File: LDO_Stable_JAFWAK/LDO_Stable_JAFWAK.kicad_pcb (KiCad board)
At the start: 4 copper layers, 1 part, among them U1 SU272AFJK_LDO

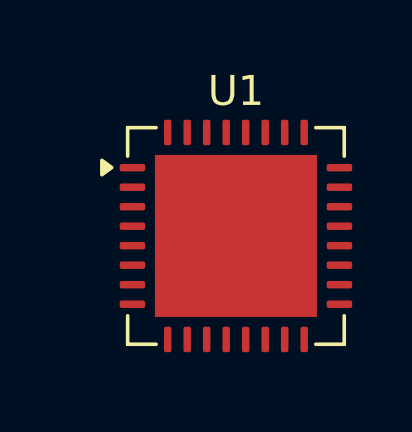
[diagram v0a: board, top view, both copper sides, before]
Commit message: Updated pin assignments on footprint
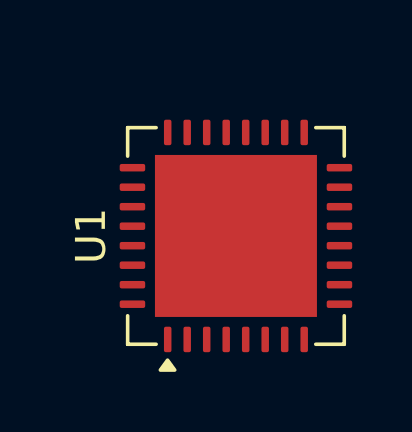
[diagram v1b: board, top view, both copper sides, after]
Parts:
- turned U1 to 90 degrees
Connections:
- U1 pad 1: BGR_VDD -> EN_VDD
- U1 pad 10: BGR_VDD -> VSS
- U1 pad 11: Net-(U1-EN_AIN) -> OTA_VDD
- U1 pad 12: Net-(U1-EN_AIN) -> OTA_VDD
- U1 pad 13: Net-(U1-EN_AIN) -> Net-(U1-VOUT-Pad13)
- U1 pad 14: Net-(U1-EN_AIN) -> Net-(U1-VOUT-Pad13)
- U1 pad 15: Net-(U1-EN_AIN) -> VSS
- U1 pad 16: BGR_VDD -> VDD
- U1 pad 17: BGR_VDD -> VDD
- U1 pad 18: BGR_VDD -> VDD
- U1 pad 19: BGR_VDD -> VDD
- U1 pad 2: BGR_VDD -> EN_VDD
- U1 pad 20: BGR_VDD -> VSS
- U1 pad 21: Net-(U1-EN_AIN) -> unconnected-(U1-VREF_IN-Pad21)
- U1 pad 22: Net-(U1-EN_AIN) -> VSS
- U1 pad 23: BGR_VDD -> unconnected-(U1-VREF_OUT-Pad23)
- U1 pad 24: BGR_VDD -> VDD
- U1 pad 27: BGR_VDD -> unconnected-(U1-VMIRROR-Pad27)
- U1 pad 28: BGR_VDD -> VSS
- U1 pad 29: Net-(U1-EN_AIN) -> VSS
- U1 pad 3: Net-(U1-EN_AIN) -> unconnected-(U1-EN_AIN-Pad3)
- U1 pad 30: BGR_VDD -> VSS
- U1 pad 31: Net-(U1-EN_AIN) -> VSS
- U1 pad 32: BGR_VDD -> VDD
- U1 pad 4: BGR_VDD -> unconnected-(U1-EN_OUT-Pad4)
- U1 pad 5: BGR_VDD -> unconnected-(U1-~{EN_OUT}-Pad5)
- U1 pad 6: BGR_VDD -> unconnected-(U1-~{EN_IN}-Pad6)
- U1 pad 7: BGR_VDD -> unconnected-(U1-EN_IN-Pad7)
- U1 pad 8: BGR_VDD -> VDD
- U1 pad 9: BGR_VDD -> VSS

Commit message: Built out primary systems
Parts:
- added C1: 0.1nF, Capacitor_SMD:C_0805_2012Metric_Pad1.18x1.45mm_HandSolder, F.Cu at (31.2, 12.7)
- added C10: 1nF, Capacitor_SMD:C_0805_2012Metric_Pad1.18x1.45mm_HandSolder, F.Cu at (40.8, 15.7)
- added C11: 100uF, TPS7A7001_Evaluation_Board_footprint_lib:CAPPRD350W60D800H1150, F.Cu at (34.2, 28.0)
- added C12: 1nF, Capacitor_SMD:C_0805_2012Metric_Pad1.18x1.45mm_HandSolder, F.Cu at (40.8, 18.7)
- added C13: 10uF, Capacitor_SMD:C_0805_2012Metric_Pad1.18x1.45mm_HandSolder, F.Cu at (40.8, 21.7)
- added C2: 100nF, Capacitor_SMD:C_0805_2012Metric_Pad1.18x1.45mm_HandSolder, F.Cu at (31.2, 15.7)
- added C3: 10uF, Capacitor_SMD:C_0805_2012Metric_Pad1.18x1.45mm_HandSolder, F.Cu at (31.2, 18.7)
- added C4: 10uF, Capacitor_SMD:C_0805_2012Metric_Pad1.18x1.45mm_HandSolder, F.Cu at (31.2, 21.7)
- added C5: 100nF, Capacitor_SMD:C_0805_2012Metric_Pad1.18x1.45mm_HandSolder, F.Cu at (36.0, 12.7)
- added C6: 0.1nF, Capacitor_SMD:C_0805_2012Metric_Pad1.18x1.45mm_HandSolder, F.Cu at (36.0, 15.7)
- added C7: OPEN, Capacitor_SMD:C_0805_2012Metric_Pad1.18x1.45mm_HandSolder, F.Cu at (36.0, 18.7)
- added C8: 1nF, Capacitor_SMD:C_0805_2012Metric_Pad1.18x1.45mm_HandSolder, F.Cu at (36.0, 21.7)
- added C9: 1nF, Capacitor_SMD:C_0805_2012Metric_Pad1.18x1.45mm_HandSolder, F.Cu at (40.8, 12.7)
- added H1: MountingHole, MountingHole:MountingHole_2.5mm, F.Cu at (11.8, 14.5)
- added H2: MountingHole, MountingHole:MountingHole_2.5mm, F.Cu at (11.8, 21.0)
- added H3: MountingHole, MountingHole:MountingHole_2.5mm, F.Cu at (11.8, 27.6)
- added H4: MountingHole, MountingHole:MountingHole_2.5mm, F.Cu at (11.8, 34.1)
- added J11: TMP_OUT, TPS7A7001_Evaluation_Board_footprint_lib:CONN_PxC02S_SUL, F.Cu at (19.4, 24.5)
- added J13: V_SIG, TPS7A7001_Evaluation_Board_footprint_lib:SAMTEC_SMA-J-P-H-ST-TH1, F.Cu at (4.01, 42.8)
- added J5: FILT_IN, TPS7A7001_Evaluation_Board_footprint_lib:CONN_PxC02S_SUL, F.Cu at (19.4, 14.2)
- added J6: FILT_OUT, TPS7A7001_Evaluation_Board_footprint_lib:CONN_PxC02S_SUL, F.Cu at (19.4, 19.4)
- added J7: IN_S, TPS7A7001_Evaluation_Board_footprint_lib:SAMTEC_SMA-J-P-H-ST-TH1, F.Cu at (4.01, 15.7)
- added J8: OUT_S, TPS7A7001_Evaluation_Board_footprint_lib:SAMTEC_SMA-J-P-H-ST-TH1, F.Cu at (4.01, 24.8)
- added J9: FILT_IN_S, TPS7A7001_Evaluation_Board_footprint_lib:SAMTEC_SMA-J-P-H-ST-TH1, F.Cu at (4.01, 33.8)
- added JP1: PEC03SAAN, TPS7A7001_Evaluation_Board_footprint_lib:CONN_PEC03SAAN_SUL, F.Cu at (39.9, 34.9)
- added JP2: TMP, TPS7A7001_Evaluation_Board_footprint_lib:CONN_PxC02S_SUL, F.Cu at (19.4, 29.7)
- added JP3: BW_ADJ, TPS7A7001_Evaluation_Board_footprint_lib:CONN_PxC02S_SUL, F.Cu at (19.4, 34.8)
- added R1: R, Package_DIP:DIP-8_W7.62mm, F.Cu at (1.08, 1.54)
- added R10: 10k, Resistor_SMD:R_0805_2012Metric_Pad1.20x1.40mm_HandSolder, F.Cu at (26.4, 21.5)
- added R11: 10k, Resistor_SMD:R_0805_2012Metric_Pad1.20x1.40mm_HandSolder, F.Cu at (26.4, 24.5)
- added R12: 30k, Resistor_SMD:R_0805_2012Metric_Pad1.20x1.40mm_HandSolder, F.Cu at (26.4, 27.4)
- added R13: 30k, Resistor_SMD:R_0805_2012Metric_Pad1.20x1.40mm_HandSolder, F.Cu at (26.4, 30.4)
- added R14: 100m, Resistor_SMD:R_2512_6332Metric_Pad1.40x3.35mm_HandSolder, F.Cu at (33.3, 40.2)
- added R15: 0, Resistor_SMD:R_0805_2012Metric_Pad1.20x1.40mm_HandSolder, F.Cu at (26.4, 33.3)
- added R2: R, Package_DIP:DIP-8_W7.62mm, F.Cu at (11.9, 1.54)
- added R3: R, Package_DIP:DIP-8_W7.62mm, F.Cu at (22.6, 1.54)
- added R4: R, Package_DIP:DIP-8_W7.62mm, F.Cu at (33.4, 1.54)
- added R5: R, Package_DIP:DIP-8_W7.62mm, F.Cu at (44.2, 1.54)
- added R6: 10k, Resistor_SMD:R_0805_2012Metric_Pad1.20x1.40mm_HandSolder, F.Cu at (26.4, 12.7)
- added R7: 10k, Resistor_SMD:R_0805_2012Metric_Pad1.20x1.40mm_HandSolder, F.Cu at (26.4, 15.6)
- added R8: 10k, Resistor_SMD:R_0805_2012Metric_Pad1.20x1.40mm_HandSolder, F.Cu at (26.4, 18.6)
- added R9: 100m, Resistor_SMD:R_2512_6332Metric_Pad1.40x3.35mm_HandSolder, F.Cu at (33.3, 35.3)
- added U2: TMP235A2DBZR, TPS7A7001_Evaluation_Board_footprint_lib:DBZ0003A-IPC_A, F.Cu at (50.3, 25.3)
- added U3: TPS7A7001DDAR, TPS7A7001_Evaluation_Board_footprint_lib:DDA0008E-IPC_A, F.Cu at (42.8, 41.0)
- added U4: BUF634AIDR, TPS7A7001_Evaluation_Board_footprint_lib:SOIC127P599X175-8N, F.Cu at (43.7, 26.5)
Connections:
- U1 pad 27: unconnected-(U1-VMIRROR-Pad27) -> VDD

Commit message: Roughed In schematic
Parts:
- removed C10, C8, C9: 1nF, Capacitor_SMD:C_0805_2012Metric_Pad1.18x1.45mm_HandSolder
- removed C4: 10uF, Capacitor_SMD:C_0805_2012Metric_Pad1.18x1.45mm_HandSolder
- removed C5: 100nF, Capacitor_SMD:C_0805_2012Metric_Pad1.18x1.45mm_HandSolder
- removed J11: TMP_OUT, TPS7A7001_Evaluation_Board_footprint_lib:CONN_PxC02S_SUL
- removed J13: V_SIG, TPS7A7001_Evaluation_Board_footprint_lib:SAMTEC_SMA-J-P-H-ST-TH1
- removed J7: IN_S, TPS7A7001_Evaluation_Board_footprint_lib:SAMTEC_SMA-J-P-H-ST-TH1
- removed J9: FILT_IN_S, TPS7A7001_Evaluation_Board_footprint_lib:SAMTEC_SMA-J-P-H-ST-TH1
- removed JP1: PEC03SAAN, TPS7A7001_Evaluation_Board_footprint_lib:CONN_PEC03SAAN_SUL
- removed R1, R2, R3, R4, R5: R, Package_DIP:DIP-8_W7.62mm
- removed R11, R6, R7, R8: 10k, Resistor_SMD:R_0805_2012Metric_Pad1.20x1.40mm_HandSolder
- removed R15: 0, Resistor_SMD:R_0805_2012Metric_Pad1.20x1.40mm_HandSolder
- removed U3: TPS7A7001DDAR, TPS7A7001_Evaluation_Board_footprint_lib:DDA0008E-IPC_A
- removed U4: BUF634AIDR, TPS7A7001_Evaluation_Board_footprint_lib:SOIC127P599X175-8N
- added C14: 100n, Capacitor_SMD:C_0805_2012Metric_Pad1.18x1.45mm_HandSolder, F.Cu at (159.3, 161.5)
- added C15: 100n, Capacitor_SMD:C_0805_2012Metric_Pad1.18x1.45mm_HandSolder, F.Cu at (143.1, 177.4)
- added C16: 100uF, TPS7A7001_Evaluation_Board_footprint_lib:CAPPRD350W60D800H1150, F.Cu at (91.3, 83.6)
- added J1: VIN_DC, TPS7A7001_Evaluation_Board_footprint_lib:CALTEST_CT3151-2, F.Cu at (81.0, 101.3)
- added J12: EN_FG, TPS7A7001_Evaluation_Board_footprint_lib:SAMTEC_SMA-J-P-H-ST-TH1, F.Cu at (113.0, 81.4)
- added J15: VOUT_BUFF, TPS7A7001_Evaluation_Board_footprint_lib:SAMTEC_SMA-J-P-H-ST-TH1, F.Cu at (167.3, 88.3)
- added J16: VDD_SEL, Connector_PinHeader_2.54mm:PinHeader_2x08_P2.54mm_Vertical, F.Cu at (116.3, 92.3)
- added J17: VS_BUFF, TPS7A7001_Evaluation_Board_footprint_lib:CALTEST_CT3151-2, F.Cu at (81.0, 87.1)
- added J18: EN_SEL, Connector_PinHeader_2.54mm:PinHeader_2x08_P2.54mm_Vertical, F.Cu at (150.4, 92.1)
- added J2: VOUT, TPS7A7001_Evaluation_Board_footprint_lib:CALTEST_CT3151-2, F.Cu at (167.9, 101.2)
- added J24: Load Cell and Buffer, Connector_PinHeader_2.54mm:PinHeader_1x02_P2.54mm_Vertical, F.Cu at (117.4, 136.7)
- added J3: GND, TPS7A7001_Evaluation_Board_footprint_lib:CALTEST_CT3151-2, F.Cu at (168.0, 115.6)
- added J4: GND, TPS7A7001_Evaluation_Board_footprint_lib:CALTEST_CT3151-2, F.Cu at (81.0, 115.6)
- added JP10: VREF, Connector_PinHeader_2.54mm:PinHeader_1x02_P2.54mm_Vertical, F.Cu at (114.0, 170.9)
- added JP11: BW_ADJ, Connector_PinHeader_2.54mm:PinHeader_1x02_P2.54mm_Vertical, F.Cu at (154.6, 162.3)
- added JP12: BW_ADJ, Connector_PinHeader_2.54mm:PinHeader_1x02_P2.54mm_Vertical, F.Cu at (138.4, 178.2)
- added R16: 10k, Resistor_SMD:R_0805_2012Metric_Pad1.20x1.40mm_HandSolder, F.Cu at (127.0, 155.0)
- added R17: 250, Resistor_SMD:R_0805_2012Metric_Pad1.20x1.40mm_HandSolder, F.Cu at (127.0, 158.0)
- added R18: 10k, Resistor_SMD:R_0805_2012Metric_Pad1.20x1.40mm_HandSolder, F.Cu at (127.0, 160.9)
- added R19: 125, Resistor_SMD:R_0805_2012Metric_Pad1.20x1.40mm_HandSolder, F.Cu at (127.0, 163.9)
- added R20: 10k, Resistor_SMD:R_0805_2012Metric_Pad1.20x1.40mm_HandSolder, F.Cu at (127.0, 166.8)
- added R21: 10k, Resistor_SMD:R_0805_2012Metric_Pad1.20x1.40mm_HandSolder, F.Cu at (127.0, 169.8)
- added R22: 125, Resistor_SMD:R_0805_2012Metric_Pad1.20x1.40mm_HandSolder, F.Cu at (131.8, 155.0)
- added R23: 10k, Resistor_SMD:R_0805_2012Metric_Pad1.20x1.40mm_HandSolder, F.Cu at (131.8, 158.0)
- added R24: 125, Resistor_SMD:R_0805_2012Metric_Pad1.20x1.40mm_HandSolder, F.Cu at (131.8, 160.9)
- added R25: 31.6, Resistor_SMD:R_0805_2012Metric_Pad1.20x1.40mm_HandSolder, F.Cu at (131.8, 163.9)
- added R26: 15.4, Resistor_SMD:R_0805_2012Metric_Pad1.20x1.40mm_HandSolder, F.Cu at (131.8, 166.8)
- added R27: 47, Resistor_SMD:R_0805_2012Metric_Pad1.20x1.40mm_HandSolder, F.Cu at (117.5, 143.0)
- added R28: 0, Resistor_SMD:R_0805_2012Metric_Pad1.20x1.40mm_HandSolder, F.Cu at (118.9, 155.0)
- added R29: 0, Resistor_SMD:R_0805_2012Metric_Pad1.20x1.40mm_HandSolder, F.Cu at (118.9, 158.0)
- added R30: 0, Resistor_SMD:R_0805_2012Metric_Pad1.20x1.40mm_HandSolder, F.Cu at (118.9, 160.9)
- added TP1: INA, TPS7A7001_Evaluation_Board_footprint_lib:KEYSTONE_5016, F.Cu at (88.1, 156.0)
- added TP10: VREF_OUT, TPS7A7001_Evaluation_Board_footprint_lib:KEYSTONE_5016, F.Cu at (94.3, 156.0)
- added TP11: TMP_OUT, TPS7A7001_Evaluation_Board_footprint_lib:KEYSTONE_5016, F.Cu at (143.9, 156.0)
- added TP12: ~{EN_IN}, TPS7A7001_Evaluation_Board_footprint_lib:KEYSTONE_5016, F.Cu at (94.3, 161.0)
- added TP13: EN_IN, TPS7A7001_Evaluation_Board_footprint_lib:KEYSTONE_5016, F.Cu at (94.3, 166.0)
- added TP2: INB, TPS7A7001_Evaluation_Board_footprint_lib:KEYSTONE_5016, F.Cu at (88.1, 161.0)
- added TP3: OUTB, TPS7A7001_Evaluation_Board_footprint_lib:KEYSTONE_5016, F.Cu at (88.1, 166.0)
- added TP4: OUTA, TPS7A7001_Evaluation_Board_footprint_lib:KEYSTONE_5016, F.Cu at (88.1, 171.0)
- added TP5: GND, TPS7A7001_Evaluation_Board_footprint_lib:KEYSTONE_5016, F.Cu at (112.0, 127.8)
- added TP6: GND, TPS7A7001_Evaluation_Board_footprint_lib:KEYSTONE_5016, F.Cu at (112.0, 132.8)
- added TP7: VIN, TPS7A7001_Evaluation_Board_footprint_lib:KEYSTONE_5016, F.Cu at (112.0, 137.8)
- added TP9: EN_AIN, TPS7A7001_Evaluation_Board_footprint_lib:KEYSTONE_5016, F.Cu at (88.1, 175.9)
- added U5: BUF634AIDR, TPS7A7001_Evaluation_Board_footprint_lib:SOIC127P599X175-8N, F.Cu at (157.0, 156.8)
- added U6: FXLP34, Package_TO_SOT_SMD:SOT-353_SC-70-5, F.Cu at (118.3, 170.4)
- added U7: BUF634AIDR, TPS7A7001_Evaluation_Board_footprint_lib:SOIC127P599X175-8N, F.Cu at (140.9, 172.7)
- added U8: FXLP34, Package_TO_SOT_SMD:SOT-353_SC-70-5, F.Cu at (118.3, 173.9)
- C13: value 10uF -> 100n
- C7: value OPEN -> 1nF
- J5: value FILT_IN -> EN_AIN_SEL; footprint TPS7A7001_Evaluation_Board_footprint_lib:CONN_PxC02S_SUL -> Connector_PinHeader_2.54mm:PinHeader_2x04_P2.54mm_Vertical
- J6: value FILT_OUT -> AD_PINS; footprint TPS7A7001_Evaluation_Board_footprint_lib:CONN_PxC02S_SUL -> Connector_PinHeader_2.54mm:PinHeader_2x08_P2.54mm_Vertical
- J8: value OUT_S -> VIN_FG
- JP2: footprint TPS7A7001_Evaluation_Board_footprint_lib:CONN_PxC02S_SUL -> Connector_PinHeader_2.54mm:PinHeader_1x02_P2.54mm_Vertical
- JP3: value BW_ADJ -> PEC03SAAN; footprint TPS7A7001_Evaluation_Board_footprint_lib:CONN_PxC02S_SUL -> Connector_PinHeader_2.54mm:PinHeader_1x03_P2.54mm_Vertical
- R12, R13: value 30k -> 10k
- moved R12 190.9 mm to (159.3, 164.5)
- moved R13 190.1 mm to (143.1, 180.4)
- moved R10 185.7 mm to (143.1, 166.0)
- moved H4 181.6 mm to (169.7, 124.0)
- moved C12 174.4 mm to (143.1, 160.0)
- moved C13 174.4 mm to (143.1, 163.0)
- moved JP2 173.5 mm to (138.4, 155.8)
- moved C6 167.6 mm to (114.1, 164.1)
- moved C7 167.6 mm to (114.1, 167.1)
- moved U2 166.8 mm to (147.9, 160.6)
- moved H3 166.1 mm to (169.7, 79.2)
- moved C1 164.7 mm to (114.1, 155.0)
- moved C2 164.7 mm to (114.1, 158.0)
- moved C3 164.7 mm to (114.1, 161.1)
- moved R14 161.9 mm to (109.1, 183.3)
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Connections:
- C1 pad 1: Net-(U3-IN) -> Net-(C1-Pad1)
- C11 pad P: /VIN -> Net-(J1-Pin_1)
- C12 pad 1: /TMP_OUT -> /TEMP
- C13 pad 1: GND -> Net-(U2-VDD)
- C13 pad 2: /VDD_BUF -> GND
- C2 pad 1: Net-(U3-IN) -> Net-(C1-Pad1)
- C3 pad 1: Net-(U3-IN) -> Net-(C1-Pad1)
- C6 pad 1: /LDO_VOUT -> Net-(C6-Pad1)
- C7 pad 1: /LDO_VOUT -> Net-(C7-Pad1)
- C7 pad 2: /FB -> GND
- J5 pad 1: Net-(J5-Pad1) -> VIN
- J5 pad 2: Net-(J5-Pad1) -> /LDO Harness/EN_AIN
- J6 pad 1: Net-(C10-Pad1) -> /ADV
- J6 pad 2: Net-(C10-Pad1) -> GND
- J8 pad 1: /VOUT -> /Buffer1/V+
- J8 pad G1: GND -> (no net)
- J8 pad G2: GND -> (no net)
- J8 pad G3: GND -> (no net)
- J8 pad G4: GND -> (no net)
- JP2 pad 1: /VIN -> /Temp Sensor/VIN
- JP3 pad 1: Net-(JP3-Pad1) -> /Buffer1/OUT
- JP3 pad 2: Net-(U4-BW) -> VIN
- R10 pad 2: /TMP_OUT -> /TEMP
- R12 pad 1: /LDO_VOUT -> GND
- R12 pad 2: /FB -> Net-(JP11-Pad1)
- R13 pad 1: /FB -> GND
- R13 pad 2: GND -> Net-(JP12-Pad1)
- R14 pad 1: /LDO_VOUT -> OUTA
- R14 pad 2: /VOUT -> VOUT
- R9 pad 1: /VIN -> VIN
- R9 pad 2: Net-(U3-IN) -> INB
- U1 pad 10: VSS -> GND
- U1 pad 13: Net-(U1-VOUT-Pad13) -> OUTA
- U1 pad 14: Net-(U1-VOUT-Pad13) -> OUTA
- U1 pad 15: VSS -> GND
- U1 pad 20: VSS -> GND
- U1 pad 21: unconnected-(U1-VREF_IN-Pad21) -> /LDO Harness/VREF_IN
- U1 pad 22: VSS -> GND
- U1 pad 23: unconnected-(U1-VREF_OUT-Pad23) -> /LDO Harness/VREF_OUT
- U1 pad 28: VSS -> GND
- U1 pad 29: VSS -> GND
- U1 pad 3: unconnected-(U1-EN_AIN-Pad3) -> /LDO Harness/EN_AIN
- U1 pad 30: VSS -> GND
- U1 pad 31: VSS -> GND
- U1 pad 4: unconnected-(U1-EN_OUT-Pad4) -> /LDO Harness/EN_OUT
- U1 pad 5: unconnected-(U1-~{EN_OUT}-Pad5) -> /LDO Harness/~{EN_OUT}
- U1 pad 6: unconnected-(U1-~{EN_IN}-Pad6) -> /LDO Harness/~{EN_IN}
- U1 pad 7: unconnected-(U1-EN_IN-Pad7) -> /LDO Harness/EN_IN
- U1 pad 9: VSS -> GND
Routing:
- added copper zone on In1.Cu, net GND
- added copper zone on In2.Cu, net VIN
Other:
- board outline added: 96.5 x 50.8 mm

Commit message: Started Layout
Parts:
- moved TP3 110.6 mm to (157.0, 79.5)
- moved R14 107.0 mm to (156.0, 87.0), turned to 90 degrees
- moved TP4 97.8 mm to (149.0, 94.5)
- moved TP9 95.4 mm to (132.5, 91.5)
- moved TP10 93.2 mm to (151.0, 82.0), turned to 90 degrees
- moved C7 91.6 mm to (147.0, 81.5), turned to 90 degrees
- moved JP10 88.0 mm to (150.0, 90.5), turned to 180 degrees
- moved R28 75.0 mm to (147.0, 85.5), turned to -90 degrees
- moved C6 74.5 mm to (148.5, 98.0)
- moved R12 69.0 mm to (161.5, 95.5)
- moved JP11 67.7 mm to (166.0, 95.5), turned to 90 degrees
- moved R29 64.8 mm to (143.5, 98.0), turned to 180 degrees
- moved R27 58.8 mm to (165.5, 109.0)
- moved R16 58.4 mm to (182.2, 136.0)
- moved R17 58.4 mm to (182.2, 138.9)
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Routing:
- net VDD: track 0.00 -> 49.1 mm, vias 0 -> 12
- net VOUT: track 0.00 -> 48.3 mm
- net /LDO Harness/EN_AIN: track 0.00 -> 30.5 mm
- net BGR_VDD: track 0.00 -> 22.4 mm, vias 0 -> 1
- net /LDO Harness/~{EN_IN}: track 0.00 -> 21.3 mm, vias 0 -> 2
- net OUTA: track 0.00 -> 20.8 mm
- net OTA_VDD: track 0.00 -> 19.7 mm, vias 0 -> 2
- net /LDO Harness/~{EN_OUT}: track 0.00 -> 18.7 mm, vias 0 -> 1
- net /LDO Harness/EN_IN: track 0.00 -> 18.0 mm
- net /LDO Harness/EN_OUT: track 0.00 -> 17.6 mm
- net EN_VDD: track 0.00 -> 16.8 mm, vias 0 -> 1
- net Net-(J12-In): track 0.00 -> 13.2 mm
- net Net-(C7-Pad1): track 0.00 -> 11.7 mm
- net Net-(U5-BW): track 0.00 -> 7.60 mm
- net VS_BUFF: track 0.00 -> 7.54 mm
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
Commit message: Save current PCB project
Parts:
- added Q10: FDV305N, FDV305N:SOT95P240X111-3N, F.Cu at (198.6, 154.1)
- added Q6: FDV305N, FDV305N:SOT95P240X111-3N, F.Cu at (198.6, 136.3)
- added Q7: FDV305N, FDV305N:SOT95P240X111-3N, F.Cu at (198.6, 140.8)
- added Q8: FDV305N, FDV305N:SOT95P240X111-3N, F.Cu at (198.6, 145.2)
- added Q9: FDV305N, FDV305N:SOT95P240X111-3N, F.Cu at (198.6, 149.7)
- moved TP11 14.1 mm to (157.5, 152.4)
- moved C13 12.5 mm to (155.2, 166.4)
- moved JP3 11.4 mm to (105.4, 152.4)
- moved JP2 8.70 mm to (144.8, 149.9)
- moved C12 7.50 mm to (135.9, 158.1)
- moved U7 5.27 mm to (146.1, 172.1)
- moved JP12 5.09 mm to (133.3, 178.2)
- moved R10 3.82 mm to (139.4, 167.0)
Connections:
- JP2 pad 1: /Temp Sensor/VIN -> VS_BUFF
- U1 pad 33: (no net) -> /LDO Harness/EP
